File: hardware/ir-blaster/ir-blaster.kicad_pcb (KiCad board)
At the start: 2 copper layers, 35 x 26 mm, 19 parts, among them J1 PWR, J2 DS18B20 [opt], Q1 DMN2046U, U1 ESP32-C3_SUPERMINI

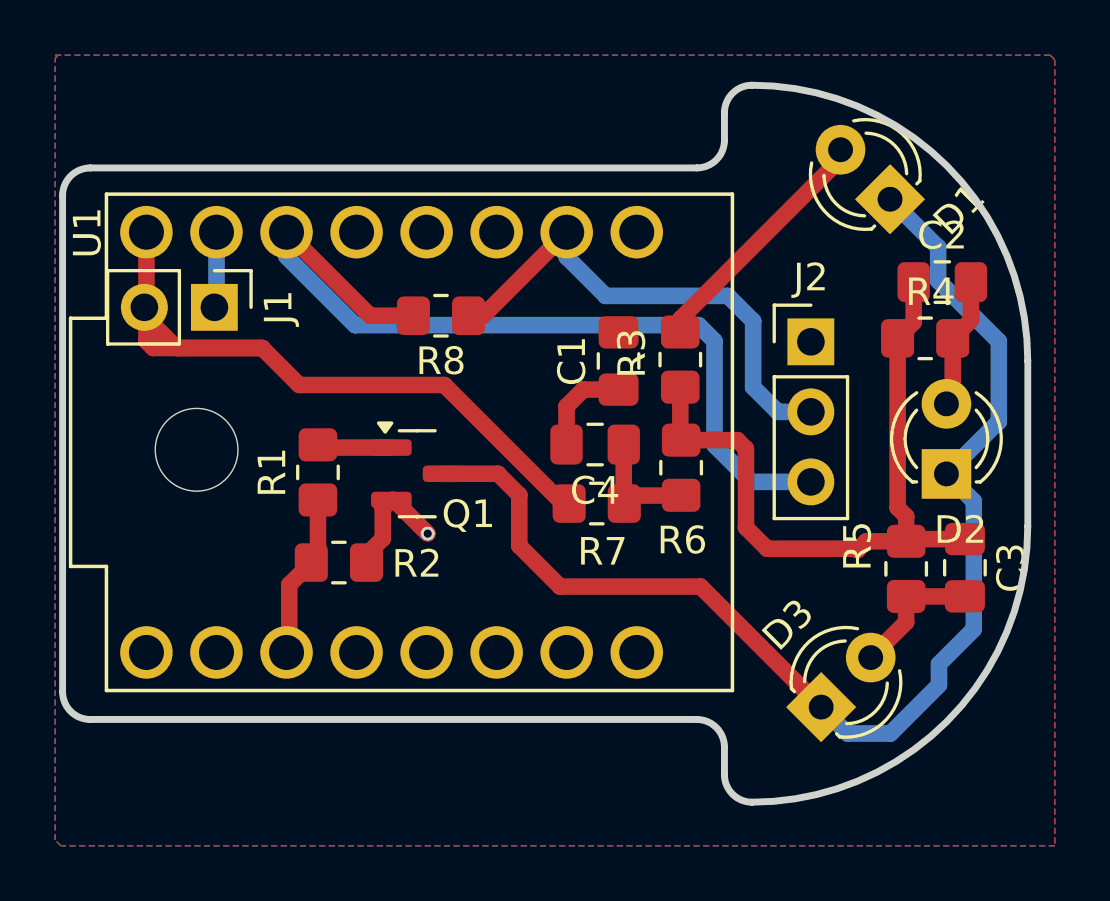
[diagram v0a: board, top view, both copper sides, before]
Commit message: added LTSpice sim
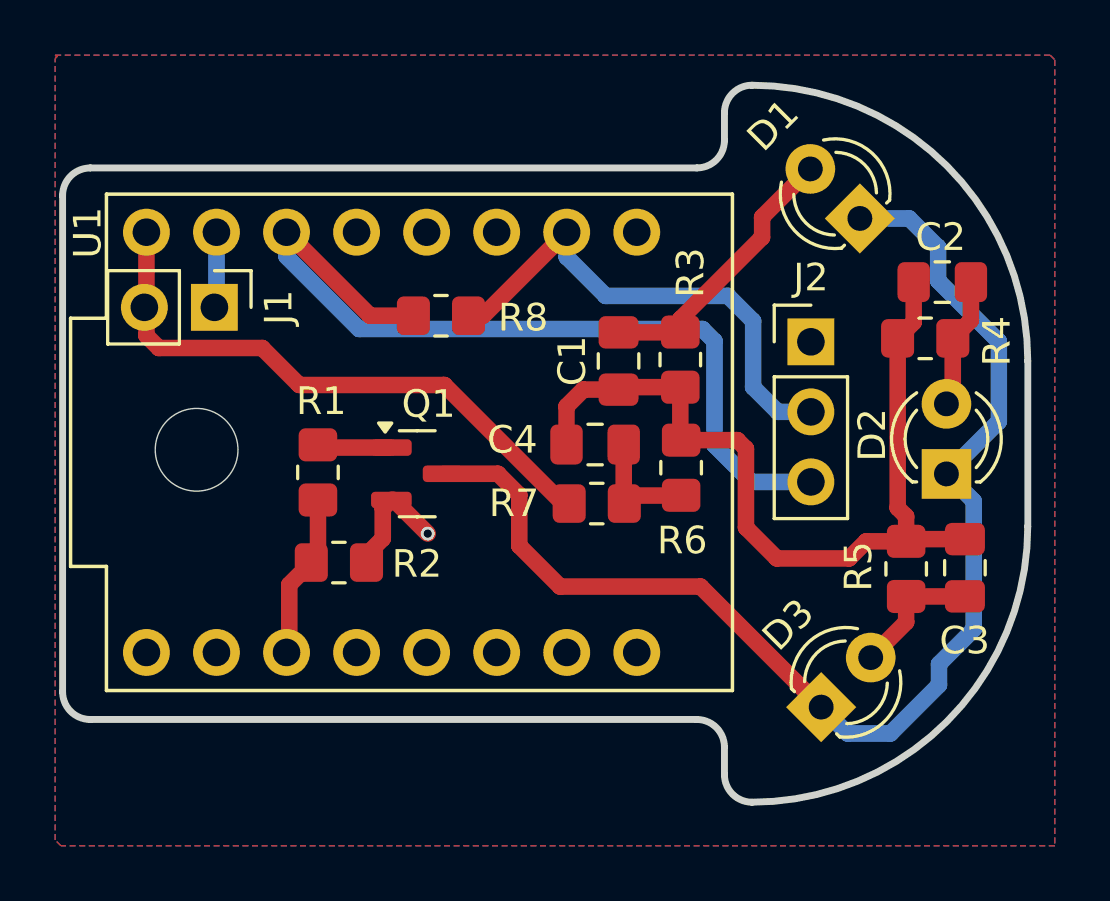
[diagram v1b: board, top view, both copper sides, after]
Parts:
- moved D1 1.30 mm to (81.8, 34.6)
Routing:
- net 5V: track 26.7 -> 21.6 mm
- net Net-(C1-Pad1): track 29.0 -> 31.5 mm
- net Net-(D1-A): track 8.54 -> 10.1 mm
- net Net-(D1-K): track 44.7 -> 45.5 mm

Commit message: New traces layout
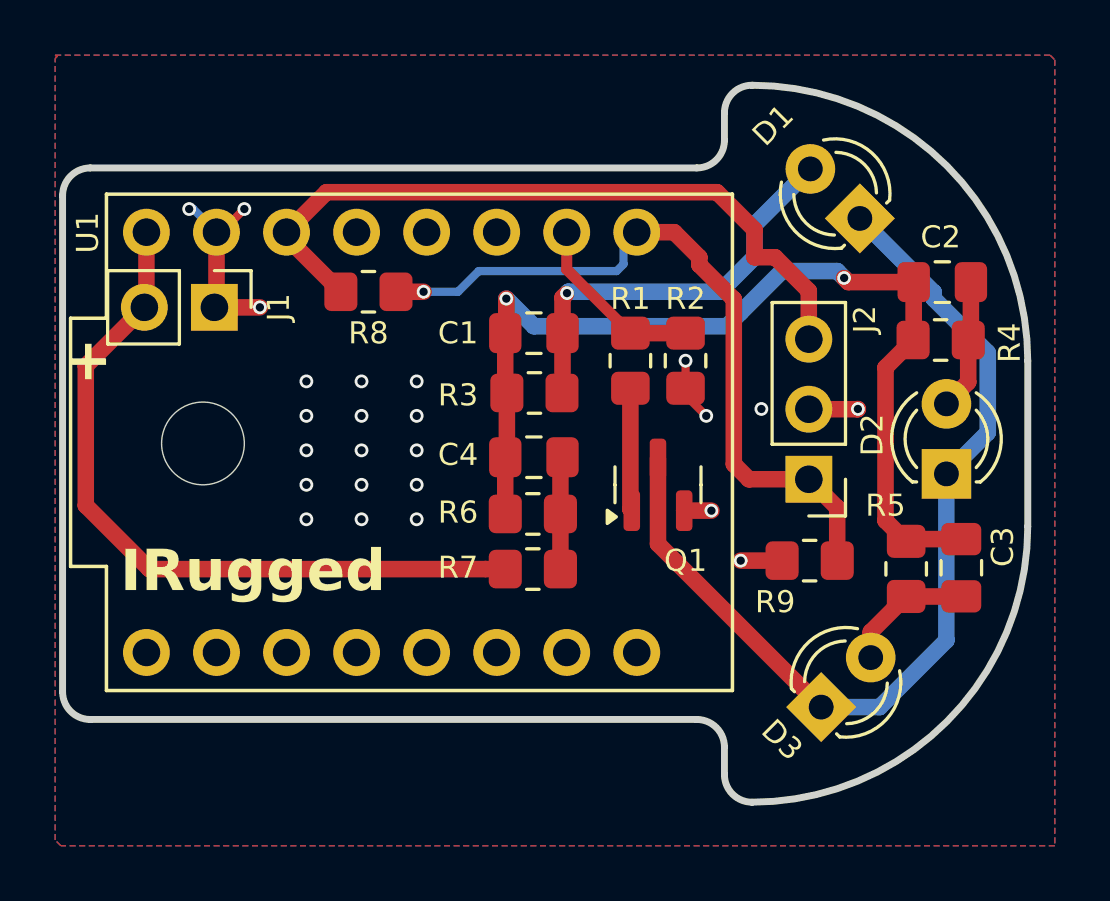
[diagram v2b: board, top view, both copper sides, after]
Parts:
- added R9: 4.7k, Resistor_SMD:R_0805_2012Metric_Pad1.20x1.40mm_HandSolder, F.Cu at (80.0, 47.0)
- C1, C2, C3, C4: value 100nF -> 220nF
- R1: value 270 -> 560
- R3, R4, R5: value 33 -> 47
- R7: value 0 -> 1
- moved R2 14.5 mm to (75.5, 39.8), turned to 90 degrees
- moved R1 12.0 mm to (73.5, 39.8), turned to -90 degrees
- moved Q1 8.74 mm to (74.5, 44.2), turned to 90 degrees
- moved R6 5.63 mm to (70.0, 45.3), turned to 0 degrees
- moved R3 5.43 mm to (70.0, 40.9), turned to 180 degrees
- moved J2 4.99 mm to (80.0, 44.0), turned to 180 degrees
- moved R7 3.32 mm to (70.0, 47.3)
- moved C1 3.23 mm to (70.0, 38.8), turned to 0 degrees
- moved R8 2.77 mm to (64.0, 37.2)
- moved C4 2.27 mm to (70.0, 43.2)
- moved R4 0.56 mm to (84.8, 39.0)
- moved C3 0.13 mm to (85.5, 47.3)
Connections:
- J2 pad 1: GND -> Net-(J2-Pin_1)
- J2 pad 2: Net-(J2-Pin_2) -> GND
- R8 pad 1: Net-(J2-Pin_2) -> Net-(J2-Pin_1)
- U1 pad 0: unconnected-(U1-GPIO0-Pad0) -> Net-(J2-Pin_1)
- U1 pad 1: Net-(J2-Pin_2) -> /IR_OUT
- U1 pad 7: /IR_OUT -> unconnected-(U1-GPIO7-Pad7)
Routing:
- net Net-(J2-Pin_1): track 0.00 -> 27.0 mm, vias 0 -> 1
- net Net-(J2-Pin_2): track 18.3 -> 0.00 mm
- net Net-(D1-K): track 45.5 -> 34.8 mm
- net GND: track 7.22 -> 13.7 mm, vias 1 -> 24
- net 5V: track 21.6 -> 27.0 mm
- net 3.3V: track 31.3 -> 26.3 mm
- net Net-(D1-A): track 10.1 -> 15.0 mm, vias 0 -> 1
- net Net-(C1-Pad1): track 31.5 -> 36.2 mm, vias 0 -> 2
- net Net-(Q1-G): track 2.70 -> 4.46 mm
- net /IR_OUT: track 6.00 -> 6.89 mm
- net Net-(D3-A): track 5.41 -> 4.75 mm
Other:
- outline, holes or cut-outs redrawn
- board text added: "+"
- board text added: "Because this is tosht"
- board text added: "IRugged"
